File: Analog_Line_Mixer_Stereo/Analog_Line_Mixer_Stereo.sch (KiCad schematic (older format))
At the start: 23 parts, among them J1 JACK-TRS, J2 JACK-TRS, J3 JACK-TRS, J4 JACK-TRS, J5 JACK-TRS, U1 LM833-N

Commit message: final commit for the night
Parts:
- C1, C2: value C -> 22pF; footprint (none) -> Capacitors_SMD:C_1206
- C3, C4: value C -> 100nF; footprint (none) -> Capacitors_SMD:C_1206
- C5, C6: value C -> 4.7uF; footprint (none) -> Capacitors_SMD:C_1206
- J1: value JACK-TRS -> IN-1
- J2: value JACK-TRS -> IN-2
- J3: value JACK-TRS -> IN-3
- J4: value JACK-TRS -> IN-4
- J5: value JACK-TRS -> OUT
- R1, R10, R2, R3, R4, R5, R6, R7, R8, R9: footprint (none) -> Resistors_SMD:R_1206
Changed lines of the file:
@@
 F 0 "U1" H 6050 2550 60  0000 C CNN
 F 1 "LM833-N" H 6150 2650 60  0000 C CNN
-F 2 "" H 6150 2650 60  0000 C CNN
+F 2 "" H 6150 2650 60  0001 C CNN
 F 3 "" H 6150 2650 60  0000 C CNN
 	1    6100 2650
@@
 F 0 "U1" H 6050 3850 60  0000 C CNN
 F 1 "LM833-N" H 6150 3950 60  0000 C CNN
-F 2 "" H 6150 3950 60  0000 C CNN
+F 2 "" H 6150 3950 60  0001 C CNN
 F 3 "" H 6150 3950 60  0000 C CNN
 	2    6100 3950
@@
 F 0 "R1" V 4080 2200 50  0000 C CNN
 F 1 "22K" V 4000 2200 50  0000 C CNN
-F 2 "" V 3930 2200 50  0000 C CNN
+F 2 "Resistors_SMD:R_1206" V 3930 2200 50  0001 C CNN
 F 3 "" H 4000 2200 50  0000 C CNN
 	1    4000 2200
@@
 F 0 "R2" V 4080 2450 50  0000 C CNN
 F 1 "22K" V 4000 2450 50  0000 C CNN
-F 2 "" V 3930 2450 50  0000 C CNN
+F 2 "Resistors_SMD:R_1206" V 3930 2450 50  0001 C CNN
 F 3 "" H 4000 2450 50  0000 C CNN
 	1    4000 2450
@@
 F 0 "R3" V 4080 3050 50  0000 C CNN
 F 1 "22K" V 4000 3050 50  0000 C CNN
-F 2 "" V 3930 3050 50  0000 C CNN
+F 2 "Resistors_SMD:R_1206" V 3930 3050 50  0001 C CNN
 F 3 "" H 4000 3050 50  0000 C CNN
 	1    4000 3050
@@
 F 0 "R4" V 4080 3300 50  0000 C CNN
 F 1 "22K" V 4000 3300 50  0000 C CNN
-F 2 "" V 3930 3300 50  0000 C CNN
+F 2 "Resistors_SMD:R_1206" V 3930 3300 50  0001 C CNN
 F 3 "" H 4000 3300 50  0000 C CNN
 	1    4000 3300
@@
 F 0 "R5" V 4080 3750 50  0000 C CNN
 F 1 "22K" V 4000 3750 50  0000 C CNN
-F 2 "" V 3930 3750 50  0000 C CNN
+F 2 "Resistors_SMD:R_1206" V 3930 3750 50  0001 C CNN
 F 3 "" H 4000 3750 50  0000 C CNN
 	1    4000 3750
@@
 F 0 "R6" V 4080 3950 50  0000 C CNN
 F 1 "22K" V 4000 3950 50  0000 C CNN
-F 2 "" V 3930 3950 50  0000 C CNN
+F 2 "Resistors_SMD:R_1206" V 3930 3950 50  0001 C CNN
 F 3 "" H 4000 3950 50  0000 C CNN
 	1    4000 3950
@@
 F 0 "R7" V 4080 4350 50  0000 C CNN
 F 1 "22K" V 4000 4350 50  0000 C CNN
-F 2 "" V 3930 4350 50  0000 C CNN
+F 2 "Resistors_SMD:R_1206" V 3930 4350 50  0001 C CNN
 F 3 "" H 4000 4350 50  0000 C CNN
 	1    4000 4350
@@
 F 0 "R8" V 4080 4550 50  0000 C CNN
 F 1 "22K" V 4000 4550 50  0000 C CNN
-F 2 "" V 3930 4550 50  0000 C CNN
+F 2 "Resistors_SMD:R_1206" V 3930 4550 50  0001 C CNN
 F 3 "" H 4000 4550 50  0000 C CNN
 	1    4000 4550
@@
 F 0 "R9" V 7630 2650 50  0000 C CNN
 F 1 "47K" V 7550 2650 50  0000 C CNN
-F 2 "" V 7480 2650 50  0000 C CNN
+F 2 "Resistors_SMD:R_1206" V 7480 2650 50  0001 C CNN
 F 3 "" H 7550 2650 50  0000 C CNN
 	1    7550 2650
@@
 F 0 "R10" V 7630 3950 50  0000 C CNN
 F 1 "47K" V 7550 3950 50  0000 C CNN
-F 2 "" V 7480 3950 50  0000 C CNN
+F 2 "Resistors_SMD:R_1206" V 7480 3950 50  0001 C CNN
 F 3 "" H 7550 3950 50  0000 C CNN
 	1    7550 3950
@@
 P 6450 3200
 F 0 "C3" H 6475 3300 50  0000 L CNN
-F 1 "C" H 6475 3100 50  0000 L CNN
-F 2 "" H 6488 3050 50  0000 C CNN
+F 1 "100nF" H 6475 3100 50  0000 L CNN
+F 2 "Capacitors_SMD:C_1206" H 6488 3050 50  0001 C CNN
 F 3 "" H 6450 3200 50  0000 C CNN
 	1    6450 3200
@@
 P 4750 3500
 F 0 "C2" H 4775 3600 50  0000 L CNN
-F 1 "C" H 4775 3400 50  0000 L CNN
-F 2 "" H 4788 3350 50  0000 C CNN
+F 1 "22pF" H 4775 3400 50  0000 L CNN
+F 2 "Capacitors_SMD:C_1206" H 4788 3350 50  0001 C CNN
 F 3 "" H 4750 3500 50  0000 C CNN
 	1    4750 3500
@@
 P 4750 3100
 F 0 "C1" H 4775 3200 50  0000 L CNN
-F 1 "C" H 4775 3000 50  0000 L CNN
-F 2 "" H 4788 2950 50  0000 C CNN
+F 1 "22pF" H 4775 3000 50  0000 L CNN
+F 2 "Capacitors_SMD:C_1206" H 4788 2950 50  0001 C CNN
 F 3 "" H 4750 3100 50  0000 C CNN
 	1    4750 3100
@@
 P 6500 2150
 F 0 "C4" H 6525 2250 50  0000 L CNN
-F 1 "C" H 6525 2050 50  0000 L CNN
-F 2 "" H 6538 2000 50  0000 C CNN
+F 1 "100nF" H 6525 2050 50  0000 L CNN
+F 2 "Capacitors_SMD:C_1206" H 6538 2000 50  0001 C CNN
 F 3 "" H 6500 2150 50  0000 C CNN
 	1    6500 2150
@@
 P 7050 2650
 F 0 "C5" H 7075 2750 50  0000 L CNN
-F 1 "C" H 7075 2550 50  0000 L CNN
-F 2 "" H 7088 2500 50  0000 C CNN
+F 1 "4.7uF" H 7075 2550 50  0000 L CNN
+F 2 "Capacitors_SMD:C_1206" H 7088 2500 50  0001 C CNN
 F 3 "" H 7050 2650 50  0000 C CNN
 	1    7050 2650
@@
 P 7050 3950
 F 0 "C6" H 7075 4050 50  0000 L CNN
-F 1 "C" H 7075 3850 50  0000 L CNN
-F 2 "" H 7088 3800 50  0000 C CNN
+F 1 "4.7uF" H 7075 3850 50  0000 L CNN
+F 2 "Capacitors_SMD:C_1206" H 7088 3800 50  0001 C CNN
 F 3 "" H 7050 3950 50  0000 C CNN
 	1    7050 3950
@@
 P 1400 2450
 F 0 "J1" H 1400 2350 60  0000 C CNN
-F 1 "JACK-TRS" H 1400 2450 60  0000 C CNN
-F 2 "" H 1400 2450 60  0000 C CNN
+F 1 "IN-1" H 1400 2450 60  0000 C CNN
+F 2 "" H 1400 2450 60  0001 C CNN
 F 3 "" H 1400 2450 60  0000 C CNN
 	1    1400 2450
@@
 P 1400 3300
 F 0 "J2" H 1400 3200 60  0000 C CNN
-F 1 "JACK-TRS" H 1400 3300 60  0000 C CNN
-F 2 "" H 1400 3300 60  0000 C CNN
+F 1 "IN-2" H 1400 3300 60  0000 C CNN
+F 2 "" H 1400 3300 60  0001 C CNN
 F 3 "" H 1400 3300 60  0000 C CNN
 	1    1400 3300
@@
 P 1400 3950
 F 0 "J3" H 1400 3850 60  0000 C CNN
-F 1 "JACK-TRS" H 1400 3950 60  0000 C CNN
-F 2 "" H 1400 3950 60  0000 C CNN
+F 1 "IN-3" H 1400 3950 60  0000 C CNN
+F 2 "" H 1400 3950 60  0001 C CNN
 F 3 "" H 1400 3950 60  0000 C CNN
 	1    1400 3950
@@
 P 1400 4550
 F 0 "J4" H 1400 4450 60  0000 C CNN
-F 1 "JACK-TRS" H 1400 4550 60  0000 C CNN
-F 2 "" H 1400 4550 60  0000 C CNN
+F 1 "IN-4" H 1400 4550 60  0000 C CNN
+F 2 "" H 1400 4550 60  0001 C CNN
 F 3 "" H 1400 4550 60  0000 C CNN
 	1    1400 4550
@@
 F 0 "RV1" H 5510 3610 50  0000 C CNN
 F 1 "MASTER_VOL" H 5640 3000 50  0000 C CNN
-F 2 "" H 5350 3300 50  0000 C CNN
+F 2 "" H 5350 3300 50  0001 C CNN
 F 3 "" H 5350 3300 50  0000 C CNN
 	1    5350 3300
@@
 P 8300 3550
 F 0 "J5" H 8300 3450 60  0000 C CNN
-F 1 "JACK-TRS" H 8300 3550 60  0000 C CNN
-F 2 "" H 8300 3550 60  0000 C CNN
+F 1 "OUT" H 8300 3550 60  0000 C CNN
+F 2 "" H 8300 3550 60  0001 C CNN
 F 3 "" H 8300 3550 60  0000 C CNN
 	1    8300 3550

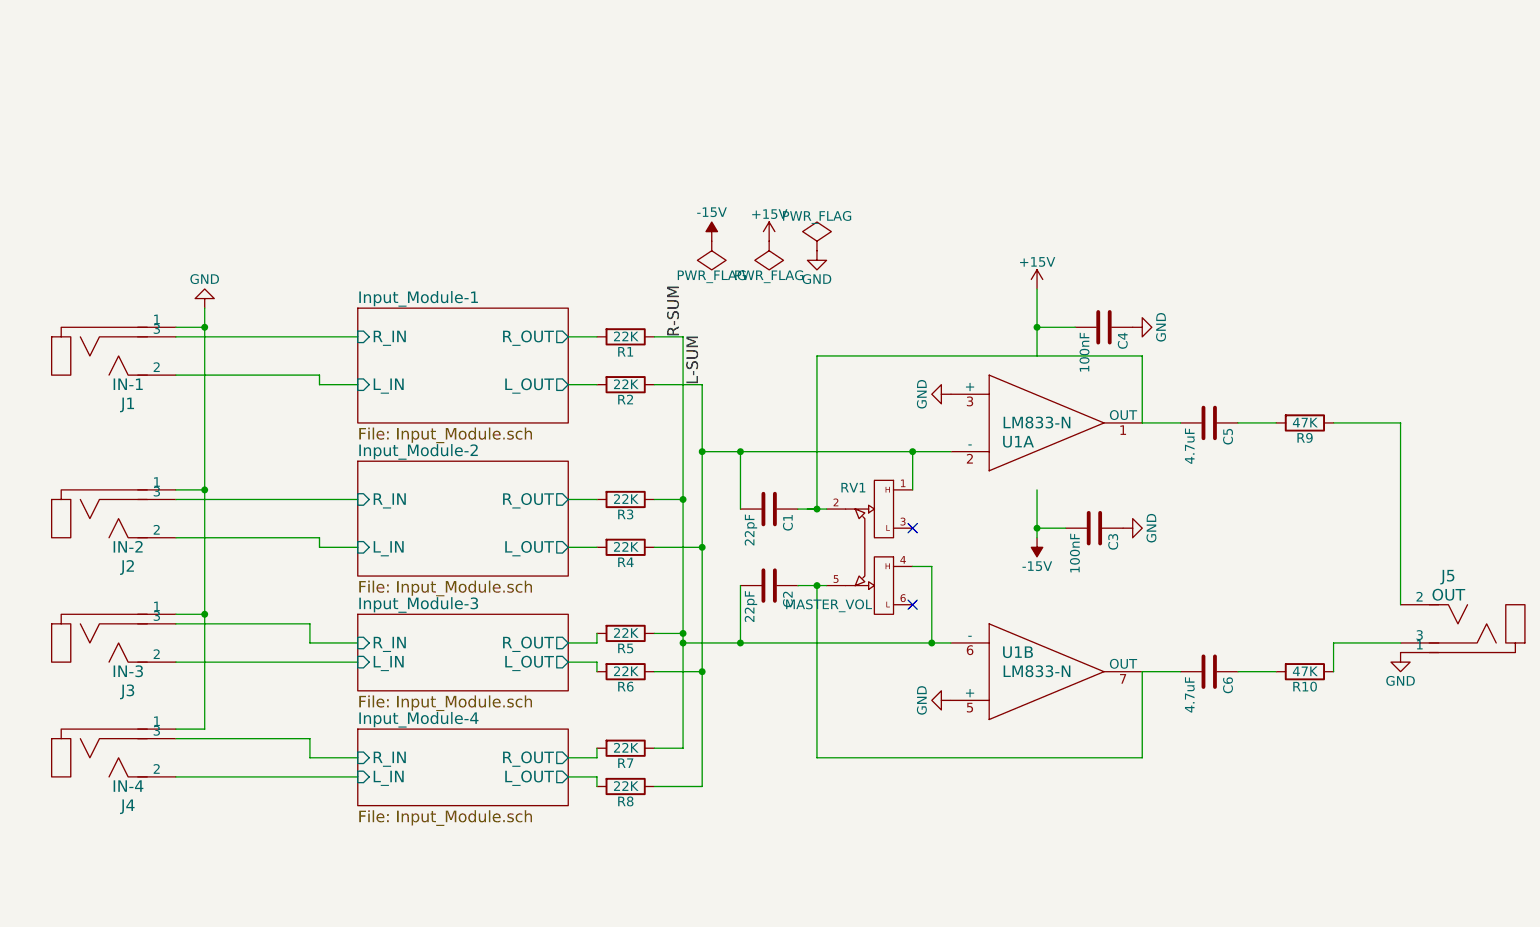
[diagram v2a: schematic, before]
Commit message: adding switches and power sources
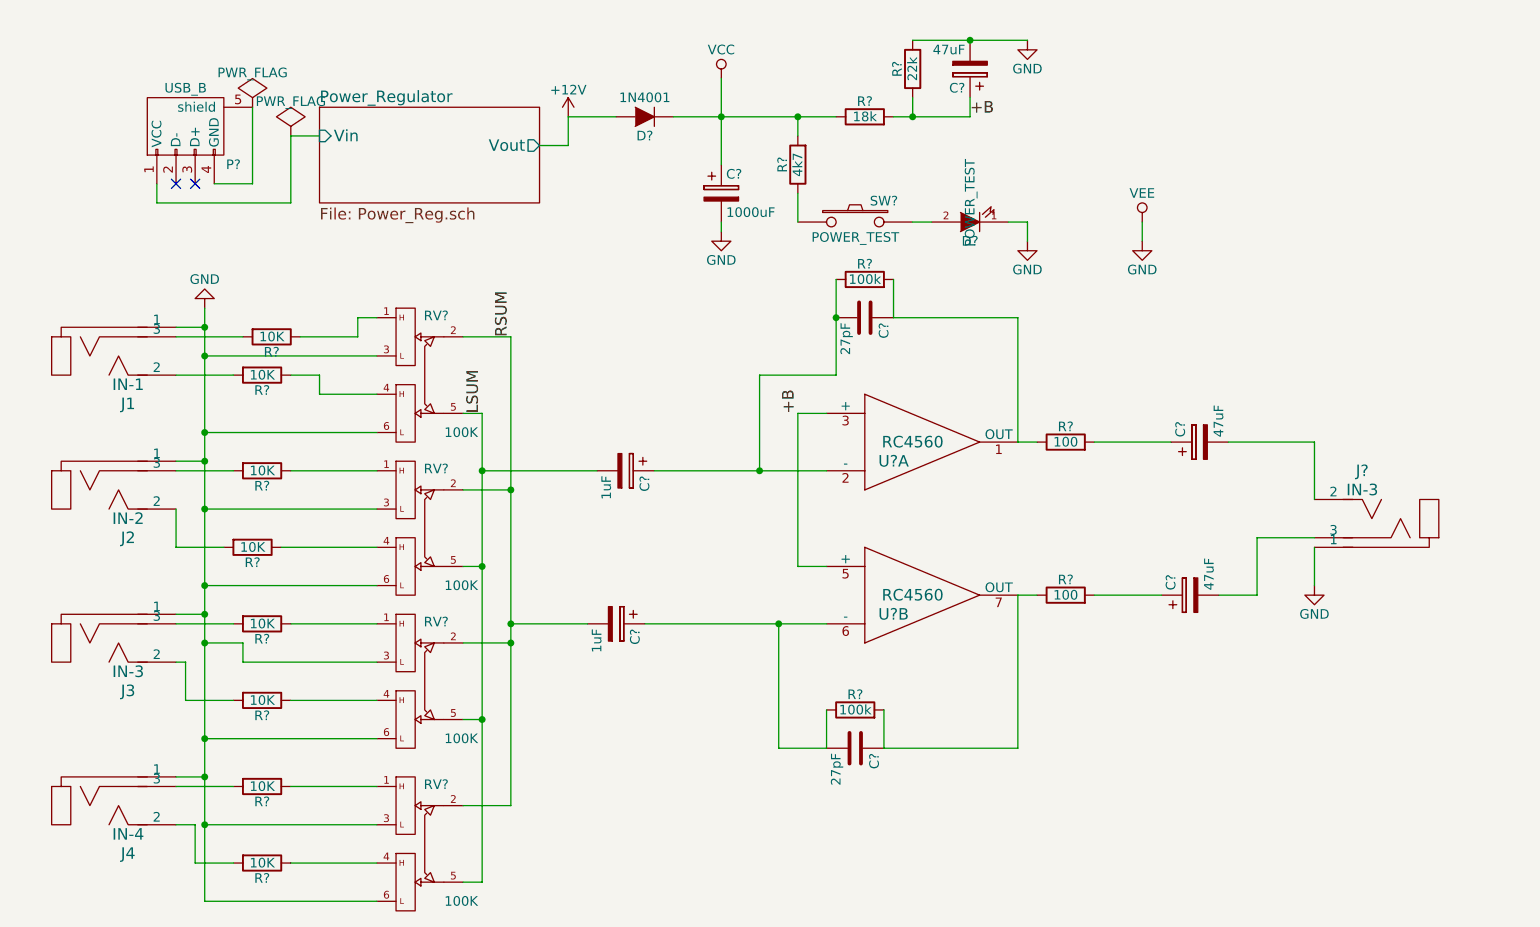
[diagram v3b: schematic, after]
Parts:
- removed C1, C2: 22pF, Capacitors_SMD:C_1206, symbol C
- removed C3, C4: 100nF, Capacitors_SMD:C_1206, symbol C
- removed C5, C6: 4.7uF, Capacitors_SMD:C_1206, symbol C
- removed J5: OUT, symbol JACK-TRS
- removed R1, R2, R3, R4, R5, R6, R7, R8: 22K, Resistors_SMD:R_1206, symbol R
- removed R10, R9: 47K, Resistors_SMD:R_1206, symbol R
- removed RV1: MASTER_VOL, symbol DUAL_POT
- removed U1: LM833-N, symbol LM833-N
- added C? (x2): 1uF, symbol CP
- added C?: 1000uF, symbol CP
- added C? (x3): 47uF, symbol CP
- added C? (x2): 27pF, symbol C
- added D?: 1N4001, symbol D
- added D?: POWER_TEST, symbol LED
- added J?: IN-3, symbol JACK-TRS
- added P?: USB_B, symbol USB_B
- added R? (x8): 10K, Resistors_SMD:R_1206, symbol R
- added R?: 4k7, Resistors_SMD:R_1206, symbol R
- added R?: 18k, Resistors_SMD:R_1206, symbol R
- added R?: 22k, Resistors_SMD:R_1206, symbol R
- added R? (x2): 100k, Resistors_SMD:R_1206, symbol R
- added R? (x2): 100, Resistors_SMD:R_1206, symbol R
- added RV? (x4): 100K, symbol DUAL_POT
- added SW?: POWER_TEST, symbol SW_PUSH
- added U? (x2): RC4560, symbol RC4560
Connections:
- net GND: now also C?.2, C?.2, D?.1 (K), J?.1, R?.2, RV?.3, RV?.3, RV?.3, RV?.3, RV?.6, RV?.6, RV?.6, RV?.6, U?.4 (VEE), U?.4 (VEE)
- net Input_Module-1/L_IN: no longer names the net of J1.2
- net Input_Module-1/L_IN: now also R?.2
- net Input_Module-1/R_IN: no longer names the net of J1.3
- net Input_Module-1/R_IN: now also R?.2
- net Input_Module-2/L_IN: no longer names the net of J2.2
- net Input_Module-2/L_IN: now also R?.2
- net Input_Module-2/R_IN: no longer names the net of J2.3
- net Input_Module-2/R_IN: now also R?.2
- net Input_Module-3/L_IN: no longer names the net of J3.2
- net Input_Module-3/L_IN: now also R?.2
- net Input_Module-3/R_IN: no longer names the net of J3.3
- net Input_Module-3/R_IN: now also R?.2
- net Input_Module-4/L_IN: no longer names the net of J4.2
- net Input_Module-4/L_IN: now also R?.2
- net Input_Module-4/R_IN: no longer names the net of J4.3
- net Input_Module-4/R_IN: now also R?.2
- new net: R?.1, RV?.1 (x4)
- new net: R?.1, RV?.4 (x4)
- new net: C?.1, C?.2, R?.1, U?.2 (-)
- new net: C?.1, C?.2, R?.1, U?.6 (-)
- new net: C?.1, R?.1, R?.2, U?.1 (OUT)
- new net: C?.1, R?.1, R?.2, U?.7 (OUT)
- new net: R?.1, SW?.1
- new net: D?.2 (A), SW?.2
- new net: C?.1, R?.2 (x2)
- new net: C?.2, J?.2
- new net: C?.2, J?.3
- new net: P?.4 (GND), P?.5 (shield)
- new net +12V: D?.2 (A)
- new net +B: C?.1, R?.1, R?.2, U?.3 (+), U?.5 (+)
- new net LSUM: C?.2, RV?.5, RV?.5, RV?.5, RV?.5
- new net Power_Regulator/Vin: P?.1 (VCC)
- new net RSUM: C?.2, RV?.2, RV?.2, RV?.2, RV?.2
- new net VCC: C?.1, D?.1 (K), R?.1, R?.2, U?.8 (VCC), U?.8 (VCC)
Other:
- moved on the sheet: J2, J4

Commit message: finalized schematic and started on board
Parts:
- added CON1: BARREL_JACK, CUI-INC:Barrel_Jack_2.1x5.5mm_CUI_INC, symbol BARREL_JACK
- added D1: 1N4001, Diodes_SMD:SOD-323, symbol D
- added SW2: Power Selector, Grayhill:Grayhill-47B-switches-SPDT-M6, symbol SWITCH_INV_MSM
- C1, C2, C3, C4, C5, C6, C7, C8: renamed from C?; footprint (none) -> Capacitors_SMD:C_1206
- D2: renamed from D?; footprint (none) -> Diodes_SMD:SOD-323
- D3: renamed from D?; footprint (none) -> LEDs:LED_0603
- J1, J2, J3, J4: footprint (none) -> CUI-INC:SJ1-353XNG-5Pin
- J5: renamed from J?; value IN-3 -> OUT; footprint (none) -> CUI-INC:SJ1-353XNG-5Pin
- P1: renamed from P?; footprint (none) -> Connect:USB_Micro-B
- R9: renamed from R?; value 4k7 -> 2k
- U1: renamed from U?; footprint (none) -> TI-R-PDSO-G8:TI-LM2698-MUA08A
- gave numbers to parts that had none: 19
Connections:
- net GND: now also P1.4 (GND), P1.5 (shield)
- net VCC: now also SW2.2; no longer D2.1 (K)
- new net: D2.1 (K), SW2.3
- new net: D1.1 (K), SW2.1
- new net: CON1.1, D1.2 (A)
- new net: CON1.2, CON1.3
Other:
- moved on the sheet: D2, P1

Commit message: mostly finalized component placement, starting routing
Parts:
- RV1, RV2, RV3, RV4: footprint (none) -> Taiwan_Alpha:TA-Dual-Pot-pin-RV122F
- SW1: footprint (none) -> Grayhill:Grayhill-38F-M6-SPST
- U1: footprint TI-R-PDSO-G8:TI-LM2698-MUA08A -> texas:TI-LM2698-MUA08A
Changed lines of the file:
@@
 F 0 "RV1" H 3010 2710 50  0000 C CNN
 F 1 "100K" H 3140 2100 50  0000 C CNN
-F 2 "" H 2850 2400 50  0001 C CNN
+F 2 "Taiwan_Alpha:TA-Dual-Pot-pin-RV122F" H 2850 2400 50  0001 C CNN
 F 3 "" H 2850 2400 50  0000 C CNN
 	1    2850 2400
@@
 F 0 "RV2" H 3010 3510 50  0000 C CNN
 F 1 "100K" H 3140 2900 50  0000 C CNN
-F 2 "" H 2850 3200 50  0001 C CNN
+F 2 "Taiwan_Alpha:TA-Dual-Pot-pin-RV122F" H 2850 3200 50  0001 C CNN
 F 3 "" H 2850 3200 50  0000 C CNN
 	1    2850 3200
@@
 F 0 "RV3" H 3010 4310 50  0000 C CNN
 F 1 "100K" H 3140 3700 50  0000 C CNN
-F 2 "" H 2850 4000 50  0001 C CNN
+F 2 "Taiwan_Alpha:TA-Dual-Pot-pin-RV122F" H 2850 4000 50  0001 C CNN
 F 3 "" H 2850 4000 50  0000 C CNN
 	1    2850 4000
@@
 F 0 "RV4" H 3010 5160 50  0000 C CNN
 F 1 "100K" H 3140 4550 50  0000 C CNN
-F 2 "" H 2850 4850 50  0001 C CNN
+F 2 "Taiwan_Alpha:TA-Dual-Pot-pin-RV122F" H 2850 4850 50  0001 C CNN
 F 3 "" H 2850 4850 50  0000 C CNN
 	1    2850 4850
@@
 F 0 "U1" H 5400 2650 60  0000 C CNN
 F 1 "RC4560" H 5500 2750 60  0000 C CNN
-F 2 "TI-R-PDSO-G8:TI-LM2698-MUA08A" H 5500 2750 60  0001 C CNN
+F 2 "texas:TI-LM2698-MUA08A" H 5500 2750 60  0001 C CNN
 F 3 "" H 5500 2750 60  0000 C CNN
 	1    5450 2750
@@
 F 0 "U1" H 5400 3450 60  0000 C CNN
 F 1 "RC4560" H 5500 3550 60  0000 C CNN
-F 2 "TI-R-PDSO-G8:TI-LM2698-MUA08A" H 5500 3550 60  0001 C CNN
+F 2 "texas:TI-LM2698-MUA08A" H 5500 3550 60  0001 C CNN
 F 3 "" H 5500 3550 60  0000 C CNN
 	2    5450 3550
@@
 F 0 "SW1" H 5350 1710 50  0000 C CNN
 F 1 "POWER_TEST" H 5200 1520 50  0000 C CNN
-F 2 "" H 5200 1600 50  0001 C CNN
+F 2 "Grayhill:Grayhill-38F-M6-SPST" H 5200 1600 50  0001 C CNN
 F 3 "" H 5200 1600 50  0000 C CNN
 	1    5200 1600

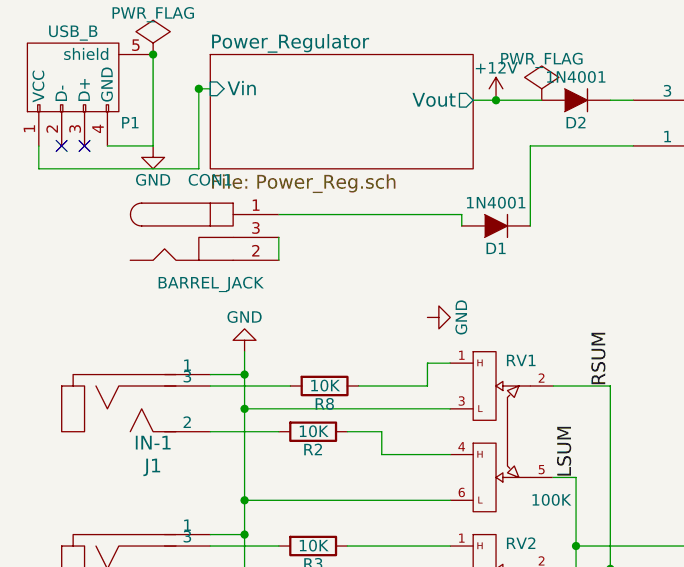
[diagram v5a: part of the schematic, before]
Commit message: routing mostly finished, need to check TSSOP package and other packages for soldermask specs
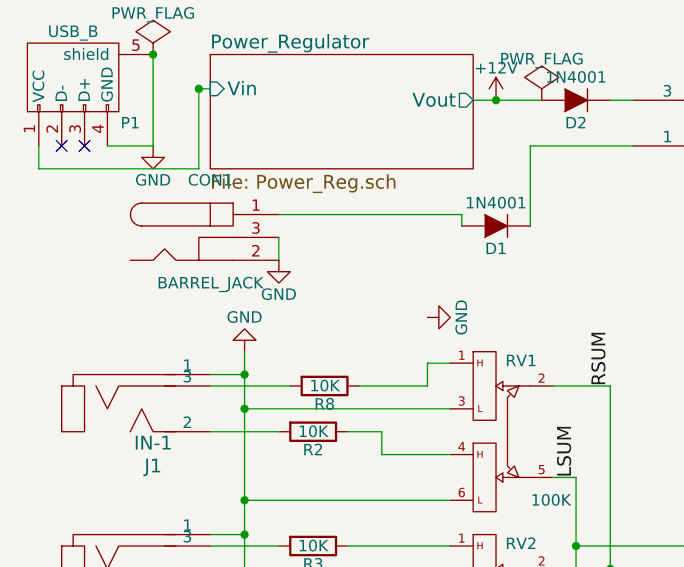
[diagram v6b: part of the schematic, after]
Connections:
- net GND: now also CON1.2, CON1.3
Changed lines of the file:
@@
 Wire Wire Line
 	3500 1150 3050 1150
+$Comp
+L GND #PWR015
+U 1 1 56B9938D
+P 1950 1650
+F 0 "#PWR015" H 1950 1400 50  0001 C CNN
+F 1 "GND" H 1950 1500 50  0000 C CNN
+F 2 "" H 1950 1650 50  0000 C CNN
+F 3 "" H 1950 1650 50  0000 C CNN
+	1    1950 1650
+	1    0    0    -1
+$EndComp
 $EndSCHEMATC
